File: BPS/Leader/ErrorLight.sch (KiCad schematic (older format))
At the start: 15 parts, among them J11 ErrorLightConn, Q3 NTR4003NT1G, Q4 VND5N07-E, U12 SI8261ABC-IS

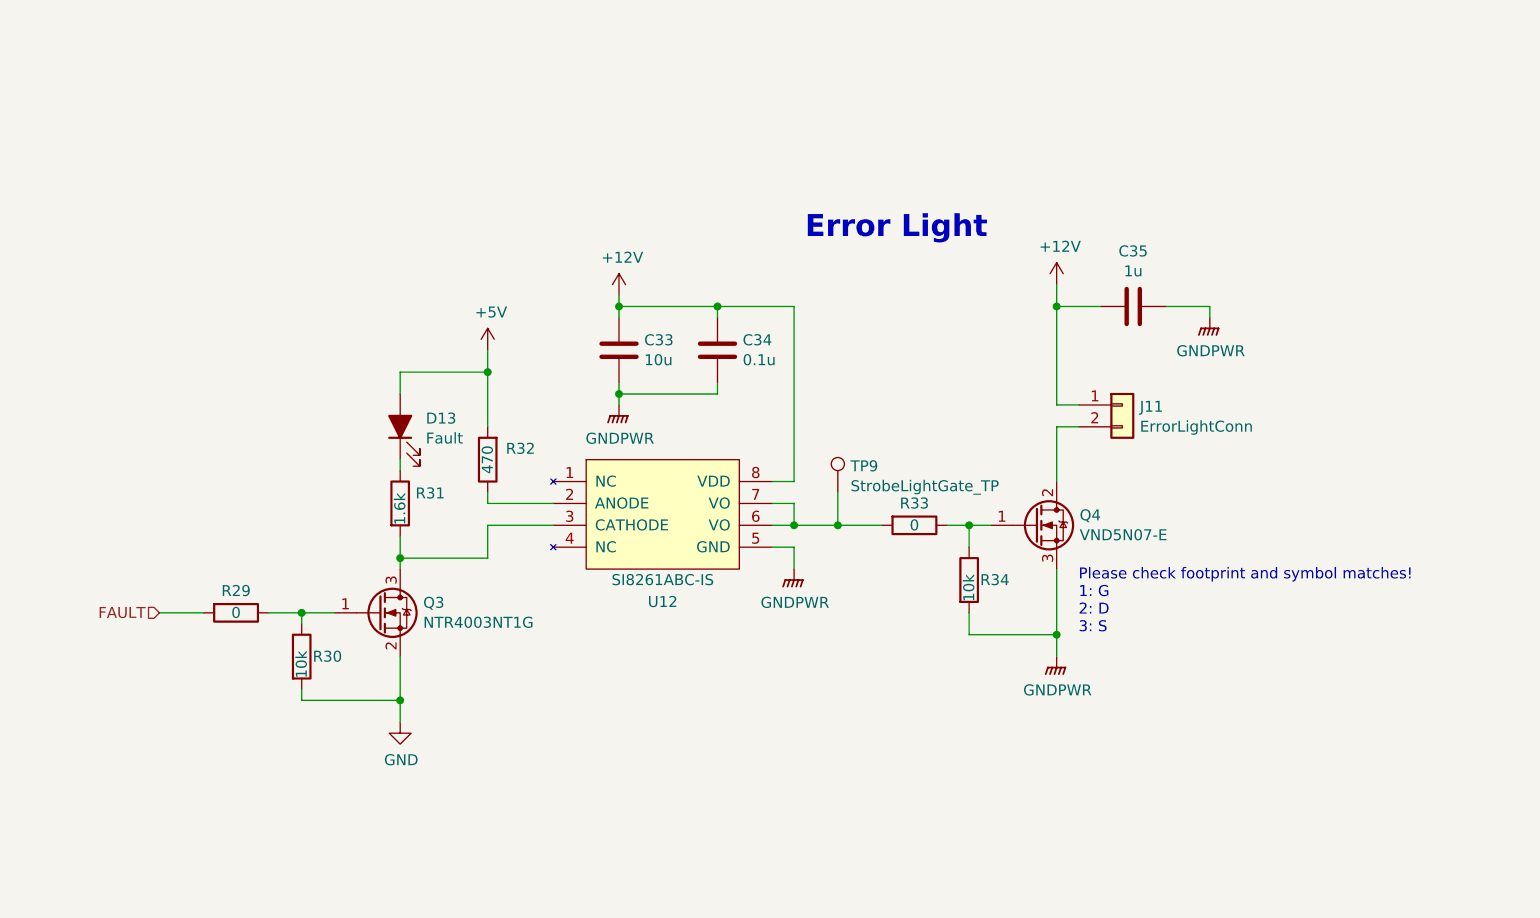
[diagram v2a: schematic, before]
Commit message: Finished leader board
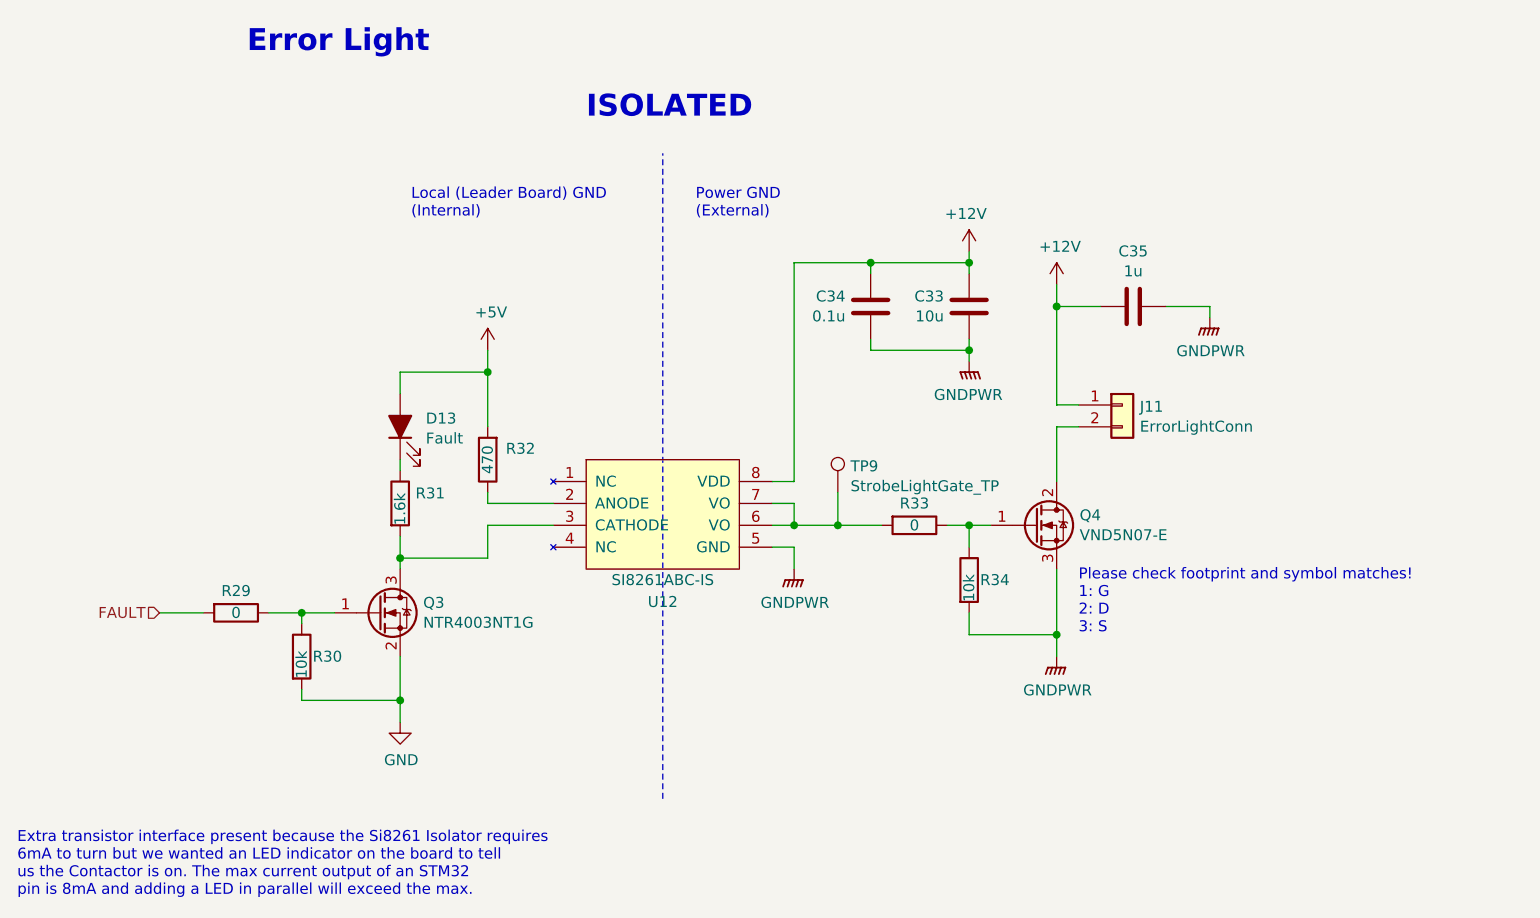
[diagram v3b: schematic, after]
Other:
- note added: "Extra transistor interface present because the Si8261 Isolator requires\n6mA to turn but we wanted an LED indicator on the board to tell\nus the Contactor is on. The max current output of an STM32\npin is 8mA and adding a LED in parallel will exceed the max."
- note added: "ISOLATED"
- note added: "Local (Leader Board) GND\n(Internal)"
- note added: "Power GND\n(External)"
- moved on the sheet: C33, C34
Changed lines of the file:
@@
 	1    0    0    -1
 $EndComp
-Text Notes 5900 2650 0    100  ~ 20
+Text Notes 3350 1800 0    100  ~ 20
 Error Light
 $Comp
@@
 L power:+12V #PWR?
 U 1 1 5D930954
-P 5050 2900
+P 6650 2700
 AR Path="/5C392C6A/5D930954" Ref="#PWR?"  Part="1"
 AR Path="/5D923D59/5D930954" Ref="#PWR068"  Part="1"
-F 0 "#PWR068" H 5050 2750 50  0001 C CNN
-F 1 "+12V" H 5065 3073 50  0000 C CNN
-F 2 "" H 5050 2900 50  0001 C CNN
-F 3 "" H 5050 2900 50  0001 C CNN
-	1    5050 2900
-	1    0    0    -1
+F 0 "#PWR068" H 6650 2550 50  0001 C CNN
+F 1 "+12V" H 6665 2873 50  0000 C CNN
+F 2 "" H 6650 2700 50  0001 C CNN
+F 3 "" H 6650 2700 50  0001 C CNN
+	1    6650 2700
+	-1   0    0    -1
 $EndComp
 $Comp
 L Device:C C?
 U 1 1 5D93095A
-P 5050 3150
+P 6650 2950
 AR Path="/5C392C6A/5D93095A" Ref="C?"  Part="1"
 AR Path="/5D923D59/5D93095A" Ref="C33"  Part="1"
-F 0 "C33" H 5165 3196 50  0000 L CNN
-F 1 "10u" H 5165 3105 50  0000 L CNN
-F 2 "Capacitor_SMD:C_0805_2012Metric" H 5088 3000 50  0001 C CNN
-F 3 "~" H 5050 3150 50  0001 C CNN
-	1    5050 3150
-	1    0    0    -1
+F 0 "C33" H 6765 2996 50  0000 L CNN
+F 1 "10u" H 6765 2905 50  0000 L CNN
+F 2 "Capacitor_SMD:C_0805_2012Metric" H 6688 2800 50  0001 C CNN
+F 3 "~" H 6650 2950 50  0001 C CNN
+	1    6650 2950
+	-1   0    0    -1
 $EndComp
 $Comp
 L power:GNDPWR #PWR?
 U 1 1 5D930960
-P 5050 3400
+P 6650 3200
 AR Path="/5C392C6A/5D930960" Ref="#PWR?"  Part="1"
 AR Path="/5D923D59/5D930960" Ref="#PWR069"  Part="1"
-F 0 "#PWR069" H 5050 3200 50  0001 C CNN
-F 1 "GNDPWR" H 5054 3246 50  0000 C CNN
-F 2 "" H 5050 3350 50  0001 C CNN
-F 3 "" H 5050 3350 50  0001 C CNN
-	1    5050 3400
-	1    0    0    -1
-$EndComp
-Wire Wire Line
-	5050 3300 5050 3350
-Wire Wire Line
-	5050 2900 5050 2950
+F 0 "#PWR069" H 6650 3000 50  0001 C CNN
+F 1 "GNDPWR" H 6654 3046 50  0000 C CNN
+F 2 "" H 6650 3150 50  0001 C CNN
+F 3 "" H 6650 3150 50  0001 C CNN
+	1    6650 3200
+	-1   0    0    -1
+$EndComp
+Wire Wire Line
+	6650 3100 6650 3150
+Wire Wire Line
+	6650 2700 6650 2750
 $Comp
 L Device:C C?
 U 1 1 5D930968
-P 5500 3150
+P 6200 2950
 AR Path="/5C392C6A/5D930968" Ref="C?"  Part="1"
 AR Path="/5D923D59/5D930968" Ref="C34"  Part="1"
-F 0 "C34" H 5615 3196 50  0000 L CNN
-F 1 "0.1u" H 5615 3105 50  0000 L CNN
-F 2 "Capacitor_SMD:C_0805_2012Metric" H 5538 3000 50  0001 C CNN
-F 3 "~" H 5500 3150 50  0001 C CNN
-	1    5500 3150
-	1    0    0    -1
-$EndComp
-Wire Wire Line
-	5500 3300 5500 3350
-Wire Wire Line
-	5500 3350 5050 3350
-Connection ~ 5050 3350
-Wire Wire Line
-	5050 3350 5050 3400
-Wire Wire Line
-	5500 3000 5500 2950
-Wire Wire Line
-	5500 2950 5050 2950
-Connection ~ 5050 2950
-Wire Wire Line
-	5050 2950 5050 3000
+F 0 "C34" H 6315 2996 50  0000 L CNN
+F 1 "0.1u" H 6315 2905 50  0000 L CNN
+F 2 "Capacitor_SMD:C_0805_2012Metric" H 6238 2800 50  0001 C CNN
+F 3 "~" H 6200 2950 50  0001 C CNN
+	1    6200 2950
+	-1   0    0    -1
+$EndComp
+Wire Wire Line
+	6200 3100 6200 3150
+Wire Wire Line
+	6200 3150 6650 3150
+Connection ~ 6650 3150
+Wire Wire Line
+	6650 3150 6650 3200
+Wire Wire Line
+	6200 2800 6200 2750
+Wire Wire Line
+	6200 2750 6650 2750
+Connection ~ 6650 2750
+Wire Wire Line
+	6650 2750 6650 2800
 Wire Wire Line
 	5750 3750 5850 3750
-Wire Wire Line
-	5850 3750 5850 2950
-Connection ~ 5500 2950
+Connection ~ 6200 2750
 $Comp
 L power:GNDPWR #PWR?
@@
 	7050 2950 7050 3400
 Wire Wire Line
-	5850 2950 5500 2950
+	5850 2750 6200 2750
 $Comp
 L utsvt-bps:SI8261ABC-IS U12
@@
 	1    0    0    -1
 $EndComp
+Wire Wire Line
+	5850 2750 5850 3750
+Wire Notes Line
+	5250 5200 5250 2250
+Text Notes 2300 5650 0    50   ~ 0
+Extra transistor interface present because the Si8261 Isolator requires\n6mA to turn but we wanted an LED indicator on the board to tell\nus the Contactor is on. The max current output of an STM32\npin is 8mA and adding a LED in parallel will exceed the max.
+Text Notes 4900 2100 0    100  ~ 20
+ISOLATED
+Text Notes 4100 2550 0    50   ~ 0
+Local (Leader Board) GND\n(Internal)
+Text Notes 5400 2550 0    50   ~ 0
+Power GND\n(External)
 $EndSCHEMATC

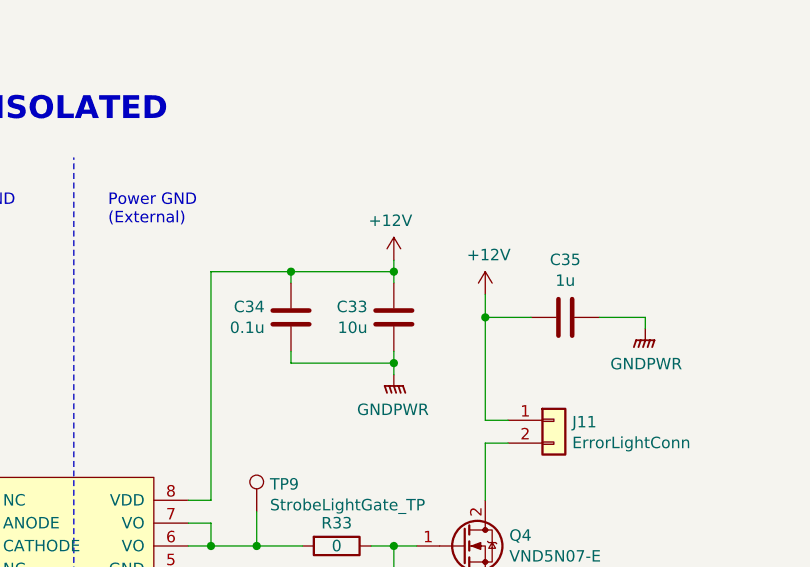
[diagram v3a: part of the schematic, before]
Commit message: Simplifies dc-dc converter schematics
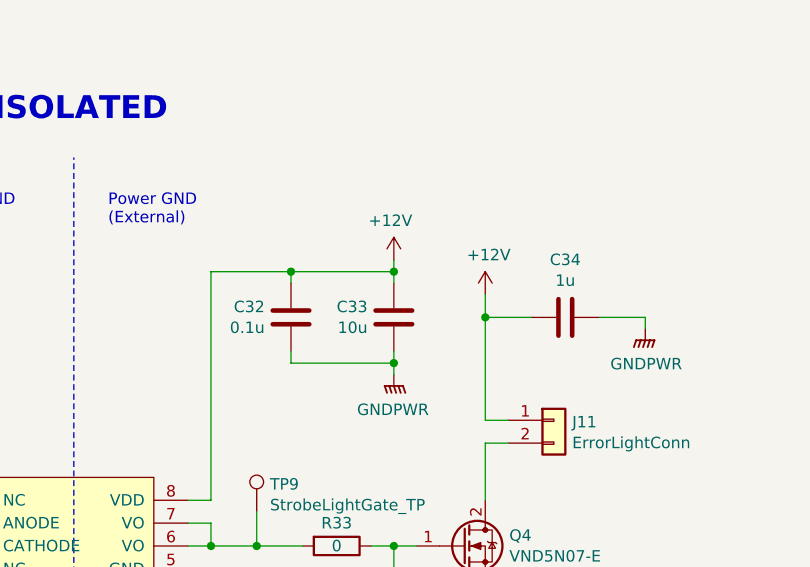
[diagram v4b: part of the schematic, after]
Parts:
- renumbered C34 to C32, C35 to C34
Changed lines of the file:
@@
 P 6200 2950
 AR Path="/5C392C6A/5D930968" Ref="C?"  Part="1"
-AR Path="/5D923D59/5D930968" Ref="C34"  Part="1"
-F 0 "C34" H 6315 2996 50  0000 L CNN
+AR Path="/5D923D59/5D930968" Ref="C32"  Part="1"
+F 0 "C32" H 6315 2996 50  0000 L CNN
 F 1 "0.1u" H 6315 2905 50  0000 L CNN
 F 2 "Capacitor_SMD:C_0805_2012Metric" H 6238 2800 50  0001 C CNN
@@
 P 5850 4150
 AR Path="/5C392C6A/5D93097A" Ref="#PWR?"  Part="1"
-AR Path="/5D923D59/5D93097A" Ref="#PWR070"  Part="1"
-F 0 "#PWR070" H 5850 3950 50  0001 C CNN
+AR Path="/5D923D59/5D93097A" Ref="#PWR067"  Part="1"
+F 0 "#PWR067" H 5850 3950 50  0001 C CNN
 F 1 "GNDPWR" H 5854 3996 50  0000 C CNN
 F 2 "" H 5850 4100 50  0001 C CNN
@@
 AR Path="/5C38C674/5D930982" Ref="#PWR?"  Part="1"
 AR Path="/5C392C6A/5D930982" Ref="#PWR?"  Part="1"
-AR Path="/5D923D59/5D930982" Ref="#PWR071"  Part="1"
-F 0 "#PWR071" H 7050 2700 50  0001 C CNN
+AR Path="/5D923D59/5D930982" Ref="#PWR070"  Part="1"
+F 0 "#PWR070" H 7050 2700 50  0001 C CNN
 F 1 "+12V" H 7065 3023 50  0000 C CNN
 F 2 "" H 7050 2850 50  0001 C CNN
@@
 AR Path="/5C38C674/5D9309BC" Ref="#PWR?"  Part="1"
 AR Path="/5C392C6A/5D9309BC" Ref="#PWR?"  Part="1"
-AR Path="/5D923D59/5D9309BC" Ref="#PWR072"  Part="1"
-F 0 "#PWR072" H 7050 4350 50  0001 C CNN
+AR Path="/5D923D59/5D9309BC" Ref="#PWR071"  Part="1"
+F 0 "#PWR071" H 7050 4350 50  0001 C CNN
 F 1 "GNDPWR" H 7054 4396 50  0000 C CNN
 F 2 "" H 7050 4500 50  0001 C CNN
@@
 AR Path="/5C38C674/5D9309C2" Ref="C?"  Part="1"
 AR Path="/5C392C6A/5D9309C2" Ref="C?"  Part="1"
-AR Path="/5D923D59/5D9309C2" Ref="C35"  Part="1"
-F 0 "C35" V 7148 2950 50  0000 C CNN
+AR Path="/5D923D59/5D9309C2" Ref="C34"  Part="1"
+F 0 "C34" V 7148 2950 50  0000 C CNN
 F 1 "1u" V 7239 2950 50  0000 C CNN
 F 2 "Capacitor_SMD:C_0805_2012Metric" H 7438 2800 50  0001 C CNN
@@
 AR Path="/5C38C674/5D9309C8" Ref="#PWR?"  Part="1"
 AR Path="/5C392C6A/5D9309C8" Ref="#PWR?"  Part="1"
-AR Path="/5D923D59/5D9309C8" Ref="#PWR073"  Part="1"
-F 0 "#PWR073" H 7750 2800 50  0001 C CNN
+AR Path="/5D923D59/5D9309C8" Ref="#PWR072"  Part="1"
+F 0 "#PWR072" H 7750 2800 50  0001 C CNN
 F 1 "GNDPWR" H 7754 2846 50  0000 C CNN
 F 2 "" H 7750 2950 50  0001 C CNN
@@
 P 4050 4850
 AR Path="/5C392C6A/5D9309F1" Ref="#PWR?"  Part="1"
-AR Path="/5D923D59/5D9309F1" Ref="#PWR066"  Part="1"
-F 0 "#PWR066" H 4050 4600 50  0001 C CNN
+AR Path="/5D923D59/5D9309F1" Ref="#PWR065"  Part="1"
+F 0 "#PWR065" H 4050 4600 50  0001 C CNN
 F 1 "GND" H 4055 4677 50  0000 C CNN
 F 2 "" H 4050 4850 50  0001 C CNN
@@
 P 4450 3150
 AR Path="/5C392C6A/5D930A01" Ref="#PWR?"  Part="1"
-AR Path="/5D923D59/5D930A01" Ref="#PWR067"  Part="1"
-F 0 "#PWR067" H 4450 3000 50  0001 C CNN
+AR Path="/5D923D59/5D930A01" Ref="#PWR066"  Part="1"
+F 0 "#PWR066" H 4450 3000 50  0001 C CNN
 F 1 "+5V" H 4465 3323 50  0000 C CNN
 F 2 "" H 4450 3150 50  0001 C CNN
